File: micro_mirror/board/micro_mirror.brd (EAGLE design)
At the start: 160 x 100 mm, 37 parts, among them IC1 7407D, IC2 7402D, IC3 74S08D, IC4 LM324D

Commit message: Layout pretty much done, need to do silkscreen.
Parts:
- added 15V_OUT, GND, GNDA, HIN0, HIN1, HIN2, HIN3, HV_ADJ, HV_IN, HV_OUT, HV_SENSE, ID0, ID1, I_SENSE_0, I_SENSE_1, LIN0, LIN1, LIN2, LIN3, PWM_0, PWM_1, PWM_2, PWM_3, SD_0, SD_1, SD_2, SD_3, VCC, VD0, VD1, VDDA, V_SENSE_0, V_SENSE_1: (no value), modular_robotics:1X04_LOCK
- added C11, C25: 10nF, rcl:C1206
- added C12, C13, C19: 2.2uF, rcl:C1206
- added C14, C15: 22uF, rcl:C1206
- added C16: 100nF 1k5V, rcl:C2225K
- added C17: 180pF, rcl:C1206
- added C18: 4.7uF, rcl:C1206
- added C20, C21, C27, C28, C32, C33: 10nF LoESL, rcl:C1206
- added C22, C29, C34: 1nF 1k5V, rcl:C1206
- added C23, C24, C30, C35: 100nF, rcl:C1206
- added C26, C31, C36: 470pF, rcl:C1206
- added D2: (no value), diode:SOD123
- added D3, D4, D5: BYG23T-M3, diode:DO214AC
- added IC5: LM324D, linear:SO14
- added J1: POWER_JACKPTH_LOCK, SparkFun-Connectors:POWER_JACK_PTH_LOCK
- added L1: 2.2uH, modular_robotics:SRN6045
- added L2: 12uH, rcl:L1812
- added R17: FUSE, rcl:R1206
- added R18: 0R, rcl:R1206
- added R19: 75k, rcl:R1206
- added R20, R25: 150k, rcl:R1206
- added R21, R39, R40: 3k3, rcl:R1206
- added R22: 2k, rcl:R1206
- added R23: 27k, rcl:R1206
- added R24: 10M, rcl:R1206
- added R26: 13k3, rcl:R1206
- added R27, R28, R44, R45, R53, R54: 100R, rcl:R1206
- added R29, R46, R55: 1M, rcl:R1206
- added R30, R35, R36, R41, R47, R56: 100k, rcl:R1206
- added R31, R33, R48, R50, R57, R59: 100M, rcl:R1206
- added R32, R34, R49, R51, R58, R60: 270k, rcl:R1206
- added R37, R38, R43, R52, R61: 1k, rcl:R1206
- added R42: FERRITE, rcl:R1206
- added U$10, U$12, U$13, U$15, U$16, U$9: HGTD1N120BNS, modular_robotics:TO252
- added U$11, U$14, U$17: IR2213, modular_robotics:SO16L
- added U$5: Q50-5C, modular_robotics:Q50-5C
- added U$6: LMR64010, modular_robotics:SOT23-5
- added U$7: LP2985-33, modular_robotics:SOT23-5
- added U$8: TPS62160, modular_robotics:TSSOP8
- C3: value 10nF 1k5V -> 1nF 1k5V
- C5: value 10nF -> 470pF
- JP2: device modular_robotics:1X04_LOCK -> pinhead:1X03
- R9: value 100R -> 1k
- moved JP2 268.8 mm to (114.3, 3.81)
- moved C9 261.8 mm to (53.3, 57.1), turned to 90 degrees
- moved C7 259.9 mm to (68.6, 57.1), turned to 90 degrees
- moved C8 248.6 mm to (38.1, 57.1), turned to 90 degrees
- moved C10 218.3 mm to (21.6, 2.54)
- moved R16 215.6 mm to (21.6, 5.71), turned to 180 degrees
- moved R15 189.0 mm to (31.8, 2.54)
- moved R14 187.3 mm to (36.8, 2.54), turned to 180 degrees
- moved R12 179.3 mm to (36.8, 10.8)
- moved C6 175.9 mm to (26.7, 2.54), turned to 180 degrees
- moved R13 174.3 mm to (21.6, 10.8)
- moved R11 171.1 mm to (36.8, 5.71), turned to 180 degrees
- moved R10 157.7 mm to (21.6, 8.26)
- moved R9 61.3 mm to (37.5, 66.0), turned to 180 degrees
- moved C5 55.4 mm to (37.5, 63.5)
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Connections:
- removed net 3V: U$1.3V
- removed net GND1: U$1.GND1
- removed net GND2: U$1.GND2
- removed net ISENSE0: C10.1, R16.2
- removed net PWM0: IC2.2, IC3.1, R9.1
- removed net SD0: U$4.13
- removed net VIN: U$1.VIN
- removed net VSENSE0: IC4.6, IC4.7, R13.1
- new net HIN1: HIN1.1, HIN1.2, HIN1.3, HIN1.4, IC3.6, U$11.12
- new net HIN2: HIN2.1, HIN2.2, HIN2.3, HIN2.4, IC3.8, U$14.12
- new net HIN3: HIN3.1, HIN3.2, HIN3.3, HIN3.4, IC3.11, U$17.12
- new net HV_ADJ: HV_ADJ.1, HV_ADJ.2, HV_ADJ.3, HV_ADJ.4, R21.2, U$1.D1
- new net HV_SENSE: HV_SENSE.1, HV_SENSE.2, HV_SENSE.3, HV_SENSE.4, R23.1, R24.2, U$1.A5
- new net ID1: IC5.10, ID1.1, ID1.2, ID1.3, ID1.4, R31.1, R32.2
- new net ID2: R48.1, R49.2
- new net ID3: R57.1, R58.2
- new net I_SENSE_0: C10.1, I_SENSE_0.1, I_SENSE_0.2, I_SENSE_0.3, I_SENSE_0.4, R16.2, U$1.A2
- new net I_SENSE_1: C25.1, I_SENSE_1.1, I_SENSE_1.2, I_SENSE_1.3, I_SENSE_1.4, R41.2, U$1.A4
- new net LIN1: IC2.4, LIN1.1, LIN1.2, LIN1.3, LIN1.4, U$11.14
- new net LIN2: IC2.10, LIN2.1, LIN2.2, LIN2.3, LIN2.4, U$14.14
- new net LIN3: IC2.13, LIN3.1, LIN3.2, LIN3.3, LIN3.4, U$17.14
- new net N$12: R17.2, U$5.2
- new net N$17: L1.1, U$8.7
- new net N$18: C14.1, HV_IN.1, HV_IN.2, HV_IN.3, HV_IN.4, L1.2, R17.1, R19.1, U$8.6
- new net N$19: C11.1, U$7.4
- new net N$20: R19.2, R20.2, U$8.5
- new net N$21: D2.A, L2.2, U$6.1
- new net N$22: R27.2, U$9.1
- new net N$23: C17.2, R25.2, R26.1, U$6.3
- new net N$24: R21.1, R22.1, U$5.6
- new net N$25: R28.2, U$10.1
- new net N$26: C20.2, R29.1, U$10.3, U$11.6, U$9.2
- new net N$27: R27.1, U$11.8
- new net N$28: R28.1, U$11.1
- new net N$29: C20.1, D3.C, U$11.7
- new net N$30: C22.1, R29.2, R30.1, R31.2
- new net N$31: IC5.8, IC5.9, R37.1
- new net N$32: IC5.2, R35.1, R38.2
- new net N$33: IC5.3, R36.1, R37.2
- new net N$34: IC5.6, IC5.7, R36.2
- new net N$35: IC5.1, R35.2, R41.1
- new net N$36: IC5.5, R39.2, R40.2
- new net N$37: C13.1, R42.2, U$7.1, U$7.3
- new net N$38: IC1.6, IC2.6, IC3.5
- new net N$39: C26.1, IC1.5, R43.2
- new net N$40: R44.2, U$12.1
- new net N$41: R45.2, U$13.1
- new net N$42: C27.2, R46.1, U$12.2, U$13.3, U$14.6
- new net N$43: R44.1, U$14.8
- new net N$44: R45.1, U$14.1
- new net N$45: C27.1, D4.C, U$14.7
- new net N$46: C29.1, R46.2, R47.1, R48.2
- new net N$47: IC1.8, IC2.9, IC3.10
- new net N$48: R53.2, U$15.1
- new net N$49: C31.1, IC1.9, R52.2
- new net N$50: R54.2, U$16.1
- new net N$51: C32.2, R55.1, U$15.2, U$16.3, U$17.6
- new net N$52: R53.1, U$17.8
- new net N$53: R54.1, U$17.1
- new net N$54: C32.1, D5.C, U$17.7
- new net N$55: C34.1, R55.2, R56.1, R57.2
- new net N$56: IC1.12, IC2.12, IC3.13
- new net N$57: C36.1, IC1.13, R61.2
- new net PWM_0: IC2.2, IC3.1, PWM_0.1, PWM_0.2, PWM_0.3, PWM_0.4, R9.1, U$1.D7
- new net PWM_1: IC2.5, IC3.4, PWM_1.1, PWM_1.2, PWM_1.3, PWM_1.4, R43.1, U$1.D6
- new net PWM_2: IC2.8, IC3.9, PWM_2.1, PWM_2.2, PWM_2.3, PWM_2.4, R52.1, U$1.D5
- new net PWM_3: IC2.11, IC3.12, PWM_3.1, PWM_3.2, PWM_3.3, PWM_3.4, R61.1, U$1.D3
- new net SD_0: SD_0.1, SD_0.2, SD_0.3, SD_0.4, U$1.D9, U$4.13
- new net SD_1: SD_1.1, SD_1.2, SD_1.3, SD_1.4, U$1.D4, U$11.13
- new net SD_2: SD_2.1, SD_2.2, SD_2.3, SD_2.4, U$1.D2, U$14.13
- new net SD_3: SD_3.1, SD_3.2, SD_3.3, SD_3.4, U$1.D0, U$17.13
- new net VCC: C15.1, C19.1, J1.PWR, L2.1, R42.1, U$1.VIN, U$6.4, U$6.5, U$8.2, U$8.3, VCC.1, VCC.2, VCC.3, VCC.4
- new net VD1: IC5.12, R33.1, R34.2, VD1.1, VD1.2, VD1.3, VD1.4
- new net VD2: R50.1, R51.2
- new net VD3: R59.1, R60.2
- new net VO2: JP2.1, R47.2, R50.2
- new net VO3: JP2.2, R56.2, R59.2
- new net V_SENSE_0: IC4.13, IC4.14, R13.1, U$1.A1, V_SENSE_0.1, V_SENSE_0.2, V_SENSE_0.3, V_SENSE_0.4
- new net V_SENSE_1: IC5.13, IC5.14, R38.1, U$1.A3, V_SENSE_1.1, V_SENSE_1.2, V_SENSE_1.3, V_SENSE_1.4
- net +15V: now also 15V_OUT.1, 15V_OUT.2, 15V_OUT.3, 15V_OUT.4, C17.1, C18.1, C21.1, C28.1, C33.1, D2.C, D3.A, D4.A, D5.A, R25.1, U$11.3, U$14.3, U$17.3
- net +3V3: now also C23.1, C30.1, C35.1, U$1.3V, U$11.11, U$14.11, U$17.11
- net GND: now also C14.2, C15.2, C16.2, C18.2, C19.2, C21.2, C22.2, C23.2, C26.2, C28.2, C29.2, C30.2, C31.2, C33.2, C34.2, C35.2, C36.2, GND.1, GND.2, GND.3, GND.4, IC1.11, IC1.3, J1.GND, J1.GNDBREAK, JP2.3, R18.1, R20.1, R22.2, R23.2, R26.2, R32.1, R34.1, R49.1, R51.1, R58.1, R60.1, U$1.GND1, U$1.GND2, U$10.2, U$11.15, U$11.2, U$13.2, U$14.15, U$14.2, U$16.2, U$17.15, U$17.2, U$5.1, U$5.4, U$6.2, U$8.1, U$8.4
- net GNDA: now also C11.2, C12.2, C13.2, C24.2, C25.2, GNDA.1, GNDA.2, GNDA.3, GNDA.4, IC5.11, R18.2, R39.1, U$7.2
- net HIN0: now also HIN0.1, HIN0.2, HIN0.3, HIN0.4
- net ID0: now also ID0.1, ID0.2, ID0.3, ID0.4
- net LIN0: now also LIN0.1, LIN0.2, LIN0.3, LIN0.4
- net N$15: now also IC4.5, R15.2; no longer IC4.12, R15.1
- net N$16: now also IC4.6, IC4.7; no longer IC4.13, IC4.14
- net V+: now also C16.1, HV_OUT.1, HV_OUT.2, HV_OUT.3, HV_OUT.4, R24.1, U$12.3, U$15.3, U$5.3, U$9.3
- net VD0: now also IC4.12, VD0.1, VD0.2, VD0.3, VD0.4; no longer IC4.5
- net VDD: now also C12.1, C24.1, IC5.4, R15.1, R40.1, U$1.AREF, U$7.5, VDDA.1, VDDA.2, VDDA.3, VDDA.4; no longer R15.2
- net VO1: now also R30.2, R33.2
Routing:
- net +15V: track 7.30 -> 197.6 mm, vias 0 -> 8
- net +3V3: track 0.00 -> 177.8 mm, vias 0 -> 8
- net VDD: track 0.00 -> 177.0 mm
- net PWM_3: track 0.00 -> 151.7 mm, vias 0 -> 3
- net PWM_2: track 0.00 -> 134.1 mm, vias 0 -> 3
- net PWM_1: track 0.00 -> 119.2 mm, vias 0 -> 3
- net PWM_0: track 0.00 -> 116.3 mm, vias 0 -> 3
- net LIN3: track 0.00 -> 114.0 mm, vias 0 -> 1
- net HIN3: track 0.00 -> 107.0 mm, vias 0 -> 3
- net VCC: track 0.00 -> 96.0 mm
- net HIN2: track 0.00 -> 93.6 mm, vias 0 -> 3
- net LIN2: track 0.00 -> 93.1 mm, vias 0 -> 3
- net V+: track 0.00 -> 79.1 mm, vias 0 -> 4
- net HIN1: track 0.00 -> 74.6 mm, vias 0 -> 1
- net ID0: track 2.54 -> 76.3 mm, vias 0 -> 1
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- added copper zone on layer 1, net GND
- added copper zone on layer 1, net GNDA
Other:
- board size 160 x 100 mm -> 127 x 76.2 mm

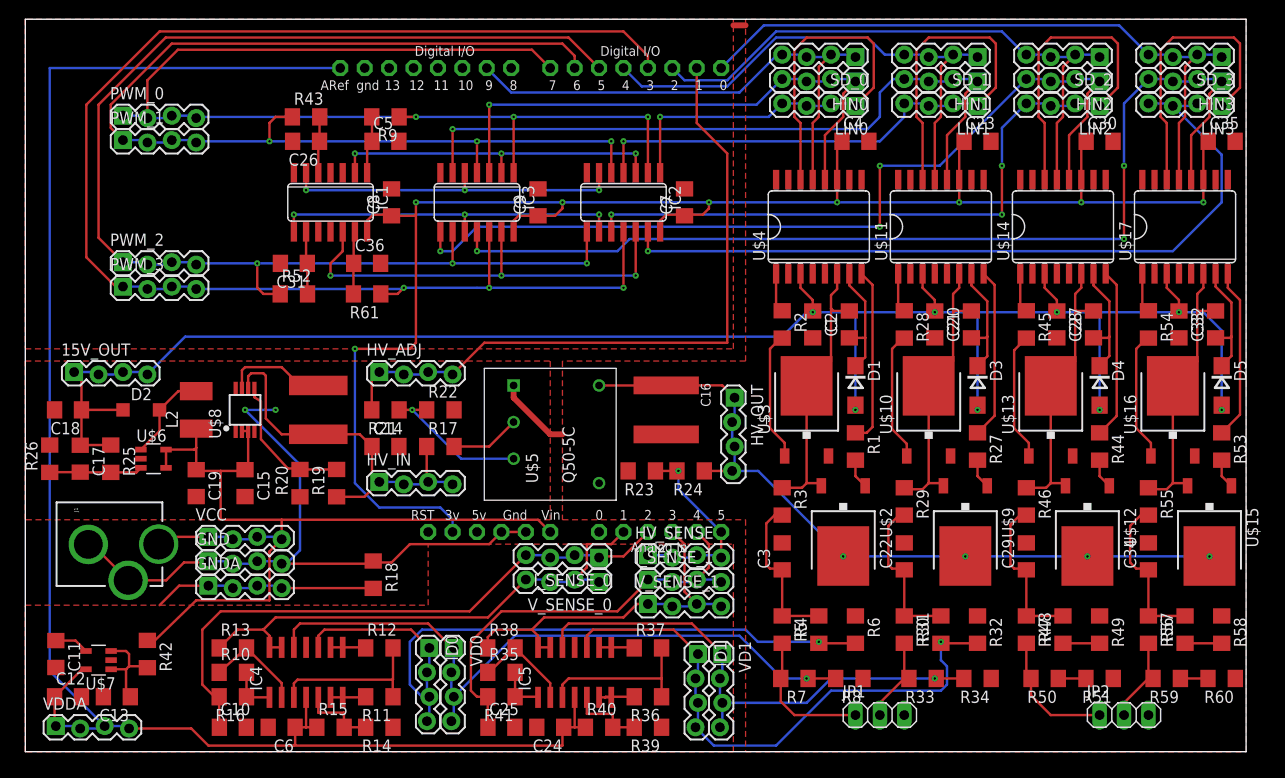
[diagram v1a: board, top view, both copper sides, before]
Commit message: Submitted micro mirror for DFM
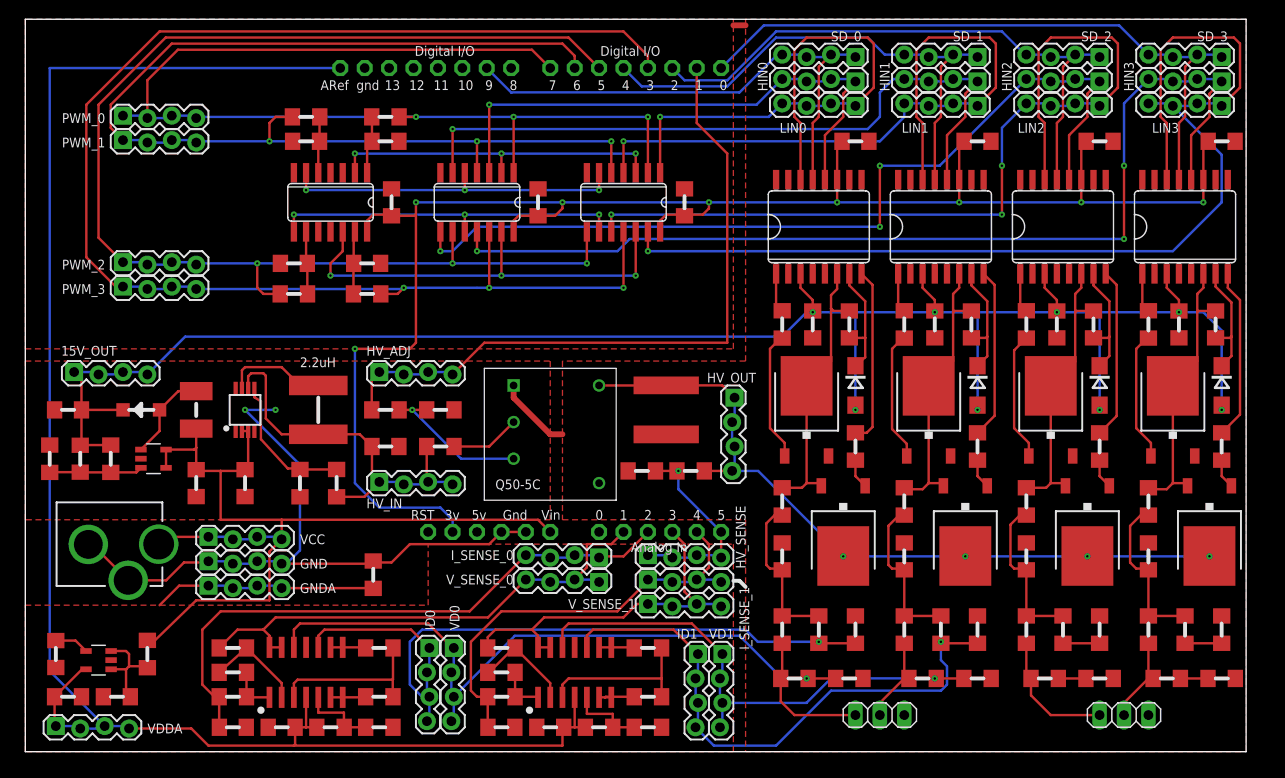
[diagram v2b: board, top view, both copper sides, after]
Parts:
- C1, C2: value 10nF LoESL -> 10nF-L
- C16: value 100nF 1k5V -> 100nF-1k5V
- C21, C28: value 10nF LoESL -> 10nF-Lo
- C3: value 1nF 1k5V -> 1nF-1k5V
- D2: value (none) -> MBR0520
- IC1: value 7407D -> 74LV7014
- IC2: value 7402D -> 74LV02
- IC3: value 74S08D -> 74LV08
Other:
- board text added: "2.2uH"

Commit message: Expanded board to enclose high voltage areas, added a few more labels
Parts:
- moved R43 0.63 mm to (29.2, 66.7)
- moved R9 0.63 mm to (37.5, 66.7)
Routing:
- net N$10: track 6.03 -> 6.66 mm
- net N$39: track 5.88 -> 6.51 mm
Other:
- board size 127 x 76.2 mm -> 128.3 x 76.2 mm
- board text added: "3.3-9V 1.5W"
- board text added: "CH0"
- board text added: "CH1"
- board text added: "CH2"
- board text added: "CH3"
- board text added: "GND"
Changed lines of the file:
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@@
 <grid distance="0.025" unitdist="inch" unit="inch" style="lines" multiple="2" display="yes" altdistance="0.005" altunitdist="inch" altunit="inch"/>
 <layers>
-<layer number="1" name="Top" color="4" fill="1" visible="yes" active="yes"/>
+<layer number="1" name="Top" color="4" fill="1" visible="no" active="yes"/>
 <layer number="2" name="Route2" color="1" fill="3" visible="no" active="no"/>
 <layer number="3" name="Route3" color="4" fill="3" visible="no" active="no"/>
@@
 <layer number="14" name="Route14" color="1" fill="6" visible="no" active="no"/>
 <layer number="15" name="Route15" color="4" fill="6" visible="no" active="no"/>
-<layer number="16" name="Bottom" color="1" fill="1" visible="no" active="yes"/>
+<layer number="16" name="Bottom" color="1" fill="1" visible="yes" active="yes"/>
 <layer number="17" name="Pads" color="2" fill="1" visible="yes" active="yes"/>
 <layer number="18" name="Vias" color="2" fill="1" visible="yes" active="yes"/>
 <layer number="19" name="Unrouted" color="6" fill="1" visible="yes" active="yes"/>
 <layer number="20" name="Dimension" color="15" fill="1" visible="yes" active="yes"/>
-<layer number="21" name="tPlace" color="7" fill="1" visible="yes" active="yes"/>
-<layer number="22" name="bPlace" color="7" fill="1" visible="no" active="yes"/>
-<layer number="23" name="tOrigins" color="15" fill="1" visible="yes" active="yes"/>
-<layer number="24" name="bOrigins" color="15" fill="1" visible="no" active="yes"/>
-<layer number="25" name="tNames" color="7" fill="1" visible="yes" active="yes"/>
+<layer number="21" name="tPlace" color="7" fill="1" visible="no" active="yes"/>
+<layer number="22" name="bPlace" color="7" fill="1" visible="yes" active="yes"/>
+<layer number="23" name="tOrigins" color="15" fill="1" visible="no" active="yes"/>
+<layer number="24" name="bOrigins" color="15" fill="1" visible="yes" active="yes"/>
+<layer number="25" name="tNames" color="7" fill="1" visible="no" active="yes"/>
 <layer number="26" name="bNames" color="7" fill="1" visible="no" active="yes"/>
-<layer number="27" name="tValues" color="7" fill="1" visible="yes" active="yes"/>
+<layer number="27" name="tValues" color="7" fill="1" visible="no" active="yes"/>
 <layer number="28" name="bValues" color="7" fill="1" visible="no" active="yes"/>
-<layer number="29" name="tStop" color="7" fill="3" visible="yes" active="yes"/>
-<layer number="30" name="bStop" color="7" fill="6" visible="no" active="yes"/>
+<layer number="29" name="tStop" color="7" fill="3" visible="no" active="yes"/>
+<layer number="30" name="bStop" color="7" fill="6" visible="yes" active="yes"/>
 <layer number="31" name="tCream" color="7" fill="4" visible="no" active="yes"/>
 <layer number="32" name="bCream" color="7" fill="5" visible="no" active="yes"/>
@@
 <layer number="37" name="tTest" color="7" fill="1" visible="no" active="yes"/>
 <layer number="38" name="bTest" color="7" fill="1" visible="no" active="yes"/>
-<layer number="39" name="tKeepout" color="4" fill="11" visible="yes" active="yes"/>
-<layer number="40" name="bKeepout" color="1" fill="11" visible="no" active="yes"/>
+<layer number="39" name="tKeepout" color="4" fill="11" visible="no" active="yes"/>
+<layer number="40" name="bKeepout" color="1" fill="11" visible="yes" active="yes"/>
 <layer number="41" name="tRestrict" color="4" fill="10" visible="no" active="yes"/>
 <layer number="42" name="bRestrict" color="1" fill="10" visible="no" active="yes"/>
@@
 <layer number="50" name="dxf" color="7" fill="1" visible="no" active="no"/>
 <layer number="51" name="tDocu" color="7" fill="1" visible="no" active="yes"/>
-<layer number="52" name="bDocu" color="7" fill="1" visible="no" active="yes"/>
+<layer number="52" name="bDocu" color="7" fill="1" visible="yes" active="yes"/>
 <layer number="53" name="tGND_GNDA" color="7" fill="9" visible="no" active="no"/>
 <layer number="54" name="bGND_GNDA" color="1" fill="9" visible="no" active="no"/>
@@
 <board>
 <plain>
-<wire x1="0" y1="0" x2="127" y2="0" width="0" layer="20"/>
-<wire x1="127" y1="0" x2="127" y2="76.2" width="0" layer="20"/>
-<wire x1="127" y1="76.2" x2="0" y2="76.2" width="0" layer="20"/>
+<wire x1="0" y1="0" x2="128.27" y2="0" width="0" layer="20"/>
+<wire x1="128.27" y1="0" x2="128.27" y2="76.2" width="0" layer="20"/>
+<wire x1="128.27" y1="76.2" x2="0" y2="76.2" width="0" layer="20"/>
 <wire x1="0" y1="76.2" x2="0" y2="0" width="0" layer="20"/>
 <wire x1="2.54" y1="31.115" x2="2.54" y2="29.845" width="0.4064" layer="21"/>
@@
 <wire x1="34.925" y1="50.8" x2="36.195" y2="50.8" width="0.4064" layer="21"/>
 <wire x1="34.925" y1="47.625" x2="36.195" y2="47.625" width="0.4064" layer="21"/>
-<wire x1="28.575" y1="66.04" x2="29.845" y2="66.04" width="0.4064" layer="21"/>
+<wire x1="28.575" y1="66.675" x2="29.845" y2="66.675" width="0.4064" layer="21"/>
 <wire x1="28.575" y1="63.5" x2="29.845" y2="63.5" width="0.4064" layer="21"/>
-<wire x1="38.1" y1="66.04" x2="36.83" y2="66.04" width="0.4064" layer="21"/>
+<wire x1="38.1" y1="66.675" x2="36.83" y2="66.675" width="0.4064" layer="21"/>
 <wire x1="38.1" y1="63.5" x2="36.83" y2="63.5" width="0.4064" layer="21"/>
 <wire x1="38.1" y1="57.785" x2="38.1" y2="56.515" width="0.4064" layer="21"/>
@@
 <wire x1="123.825" y1="7.62" x2="125.095" y2="7.62" width="0.4064" layer="21"/>
 <wire x1="36.195" y1="19.05" x2="36.195" y2="17.78" width="0.4064" layer="21"/>
+<text x="0.381" y="15.494" size="1.016" layer="21" font="vector" ratio="15">3.3-9V 1.5W</text>
+<text x="84.455" y="0.635" size="1.016" layer="21" font="vector" ratio="15">CH0</text>
+<text x="87.63" y="0.635" size="1.016" layer="21" font="vector" ratio="15">CH1</text>
+<text x="90.805" y="0.635" size="1.016" layer="21" font="vector" ratio="15">GND</text>
+<text x="109.855" y="0.635" size="1.016" layer="21" font="vector" ratio="15">CH2</text>
+<text x="113.03" y="0.635" size="1.016" layer="21" font="vector" ratio="15">CH3</text>
+<text x="116.205" y="0.635" size="1.016" layer="21" font="vector" ratio="15">GND</text>
 </plain>
 <attributes>
@@
 <attribute name="VALUE" x="49.276" y="57.658" size="1.016" layer="27" font="vector" ratio="15" rot="R180"/>
 </element>
-<element name="R9" library="rcl" package="R1206" value="1k" x="37.465" y="66.04" smashed="yes" rot="R180">
-<attribute name="VALUE" x="38.735" y="68.58" size="1.016" layer="27" font="vector" ratio="15" rot="R180"/>
+<element name="R9" library="rcl" package="R1206" value="1k" x="37.465" y="66.675" smashed="yes" rot="R180">
+<attribute name="VALUE" x="38.735" y="69.215" size="1.016" layer="27" font="vector" ratio="15" rot="R180"/>
 </element>
 <element name="C5" library="rcl" package="C1206" value="470pF" x="37.465" y="63.5" smashed="yes">
@@
 <attribute name="VALUE" x="29.21" y="68.58" size="1.016" layer="27" font="vector" ratio="15" rot="R180"/>
 </element>
-<element name="R43" library="rcl" package="R1206" value="1k" x="29.21" y="66.04" smashed="yes">
-<attribute name="VALUE" x="25.4" y="61.595" size="1.016" layer="27" font="vector" ratio="15"/>
+<element name="R43" library="rcl" package="R1206" value="1k" x="29.21" y="66.675" smashed="yes">
+<attribute name="VALUE" x="25.4" y="62.23" size="1.016" layer="27" font="vector" ratio="15"/>
 </element>
 <element name="U$12" library="modular_robotics" package="TO252" value="HGTD1N120BNS" x="110.49" y="22.86" smashed="yes" rot="R180"/>
@@
 <vertex x="74.93" y="24.13"/>
 <vertex x="74.93" y="0"/>
-<vertex x="127" y="0"/>
-<vertex x="127" y="76.2"/>
+<vertex x="128.27" y="0"/>
+<vertex x="128.27" y="75.565"/>
 </polygon>
 <contactref element="C26" pad="2"/>
@@
 <wire x1="35.56" y1="62.995" x2="36.065" y2="63.5" width="0.254" layer="1"/>
 <wire x1="36.065" y1="63.5" x2="36.065" y2="66.018" width="0.254" layer="1"/>
-<wire x1="36.065" y1="66.018" x2="36.043" y2="66.04" width="0.254" layer="1"/>
+<wire x1="36.065" y1="66.018" x2="36.043" y2="66.675" width="0.254" layer="1"/>
 </signal>
 <signal name="N$9">
@@
 <via x="40.64" y="66.04" extent="1-16" drill="0.254"/>
 <wire x1="50.8" y1="66.04" x2="40.64" y2="66.04" width="0.254" layer="16"/>
-<wire x1="40.64" y1="66.04" x2="38.887" y2="66.04" width="0.254" layer="1"/>
 <wire x1="17.78" y1="65.913" x2="17.907" y2="66.04" width="0.254" layer="16"/>
 <wire x1="17.907" y1="66.04" x2="40.64" y2="66.04" width="0.254" layer="16"/>
@@
 <wire x1="15.24" y1="66.167" x2="17.526" y2="66.167" width="0.254" layer="16"/>
 <wire x1="17.526" y1="66.167" x2="17.78" y2="65.913" width="0.254" layer="16"/>
+<wire x1="38.887" y1="66.675" x2="40.005" y2="66.675" width="0.254" layer="1"/>
+<wire x1="40.005" y1="66.675" x2="40.64" y2="66.04" width="0.254" layer="1"/>
 </signal>
 <signal name="PWM_1">
@@
 <wire x1="25.4" y1="63.5" x2="17.907" y2="63.5" width="0.254" layer="16"/>
 <wire x1="17.907" y1="63.5" x2="17.78" y2="63.373" width="0.254" layer="16"/>
-<wire x1="27.788" y1="66.04" x2="26.035" y2="66.04" width="0.254" layer="1"/>
-<wire x1="26.035" y1="66.04" x2="25.4" y2="65.405" width="0.254" layer="1"/>
 <wire x1="25.4" y1="65.405" x2="25.4" y2="63.5" width="0.254" layer="1"/>
 <via x="25.4" y="63.5" extent="1-16" drill="0.254"/>
@@
 <wire x1="8.89" y1="67.31" x2="8.89" y2="64.897" width="0.254" layer="1"/>
 <wire x1="8.89" y1="64.897" x2="10.16" y2="63.627" width="0.254" layer="1"/>
+<wire x1="25.4" y1="65.405" x2="26.67" y2="66.675" width="0.254" layer="1"/>
+<wire x1="26.67" y1="66.675" x2="27.788" y2="66.675" width="0.254" layer="1"/>
 </signal>
 <signal name="PWM_2">
@@
 <wire x1="30.48" y1="63.37" x2="30.61" y2="63.5" width="0.254" layer="1"/>
 <wire x1="30.61" y1="63.5" x2="30.61" y2="66.018" width="0.254" layer="1"/>
-<wire x1="30.61" y1="66.018" x2="30.632" y2="66.04" width="0.254" layer="1"/>
+<wire x1="30.61" y1="66.018" x2="30.632" y2="66.675" width="0.254" layer="1"/>
 </signal>
 <signal name="N$40">

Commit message: Tiled micro mirror board. Added author info etc. Used extra buffers in full channels for additional drive isolation. Added border.
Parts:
- added U$18: INFO, modular_robotics:INFO
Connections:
- new net N$58: IC1.4, IC2.5, IC3.4, R43.1
- new net N$59: IC1.10, IC2.2, IC3.1, R9.1
- net GND: no longer IC1.11, IC1.3
- net PWM_0: now also IC1.11; no longer IC2.2, IC3.1, R9.1
- net PWM_1: now also IC1.3; no longer IC2.5, IC3.4, R43.1
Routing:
- net N$59: track 0.00 -> 70.2 mm, vias 0 -> 4
- net N$58: track 0.00 -> 48.9 mm, vias 0 -> 3
- net PWM_1: track 119.4 -> 82.6 mm, vias 3 -> 1
- net PWM_0: track 116.6 -> 81.9 mm
